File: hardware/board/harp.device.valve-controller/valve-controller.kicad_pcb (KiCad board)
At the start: 4 copper layers, 80 x 168 mm, 149 parts, among them J1 Screw_Terminal_01x02, J10 Screw_Terminal_01x02, J11 Screw_Terminal_01x02, J12 Screw_Terminal_01x02, J13 Screw_Terminal_01x02, J14 Screw_Terminal_01x02, J15 Screw_Terminal_01x02, J16 Screw_Terminal_01x02, J17 Screw_Terminal_01x02, J18 Screw_Terminal_01x02, J19 Screw_Terminal_01x02, J2 Conn_01x03_Male, J20 Screw_Terminal_01x02, J3 Screw_Terminal_01x02, J4 AudioJack3, J5 USB_C_Receptacle_USB2.0, J6 Screw_Terminal_01x02, J7 Screw_Terminal_01x02, J8 Screw_Terminal_01x02, J9 Screw_Terminal_01x02, Q2 GSFD4005, U1 MIC4127, U10 MIC4127, U11 MIC4127, U12 MIC4127, U13 MIC4127, U14 MIC4127, U2 TPD2EUSB30, U3 ADUM4160, U4 RP2040, U5 W25Q16JVUXIQ, U6 MIC4127, U7 rt6150b-33gqw, U8 MIC4127, U9 MCP16312x-xMNY, X1 ECS-TXO-2016

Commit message: route pcb
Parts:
- removed G3: LOGO, LOGO
- added G***: LOGO, LOGO, B.Cu at (131.9, 166.4)
- added J26: Conn_02x10_Odd_Even, Connector_PinHeader_2.54mm:PinHeader_2x10_P2.54mm_Vertical_SMD, F.Cu at (122.8, 115.0)
- added REF**: MountingHole_3.2mm_M3_DIN965, MountingHole:MountingHole_3.2mm_M3_DIN965, F.Cu at (105.8, 181.0)
- added REF**: MountingHole_3.2mm_M3_DIN965, MountingHole:MountingHole_3.2mm_M3_DIN965, F.Cu at (105.8, 112.0)
- added REF**: MountingHole_3.2mm_M3_DIN965, MountingHole:MountingHole_3.2mm_M3_DIN965, F.Cu at (139.8, 112.0)
- J4: moved to F.Cu
- moved REF1 151.7 mm to (133.8, 180.5)
- moved C11 66.8 mm to (100.7, 102.6), turned to -90 degrees
- moved C16 61.9 mm to (108.7, 106.3), turned to 135 degrees
- moved U7 49.5 mm to (135.1, 74.6), turned to 180 degrees
- moved R15 47.6 mm to (131.4, 74.0), turned to -90 degrees
- moved C28 46.8 mm to (135.1, 77.3)
- moved R16 45.9 mm to (132.4, 74.6), turned to -90 degrees
- moved L3 45.3 mm to (137.8, 74.5), turned to -90 degrees
- moved C27 45.0 mm to (139.9, 73.6), turned to -90 degrees
- moved R20 27.6 mm to (124.8, 32.8), turned to 90 degrees
- moved C32 27.1 mm to (121.8, 34.6), turned to 90 degrees
- moved C33 25.3 mm to (128.0, 36.5), turned to -90 degrees
- moved R19 25.1 mm to (127.2, 33.5), turned to 180 degrees
- moved C30 24.0 mm to (124.6, 40.8)
- moved C31 23.4 mm to (124.6, 38.8)
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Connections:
- C20 pad 2: VPP -> +5V
- C21 pad 2: VPP -> +5V
- C22 pad 2: VPP -> +5V
- C23 pad 2: VPP -> +5V
- C24 pad 2: VPP -> +5V
- C25 pad 2: VPP -> +5V
- C26 pad 2: VPP -> +5V
- C28 pad 2: +3V3 -> +3.3V
- C29 pad 2: VPP -> +5V
- R12 pad 1: Net-(U4-GPIO24) -> Net-(U4-GPIO2)
- R13 pad 1: Net-(U4-GPIO25) -> Net-(U4-GPIO3)
- U1 pad 6: VPP -> +5V
- U10 pad 6: VPP -> +5V
- U11 pad 6: VPP -> +5V
- U12 pad 6: VPP -> +5V
- U13 pad 6: VPP -> +5V
- U14 pad 6: VPP -> +5V
- U4 pad 34: unconnected-(U4-GPIO22-Pad34) -> /Harp Core RP2040 + Isolated USB/GPIO0
- U4 pad 35: unconnected-(U4-GPIO23-Pad35) -> /Harp Core RP2040 + Isolated USB/GPIO1
- U4 pad 36: Net-(U4-GPIO24) -> /Harp Core RP2040 + Isolated USB/GPIO2
- U4 pad 37: Net-(U4-GPIO25) -> /Harp Core RP2040 + Isolated USB/GPIO3
- U4 pad 38: unconnected-(U4-GPIO26_ADC0-Pad38) -> /Harp Core RP2040 + Isolated USB/GPIO4
- U4 pad 39: unconnected-(U4-GPIO27_ADC1-Pad39) -> /Harp Core RP2040 + Isolated USB/GPIO5
- U4 pad 4: unconnected-(U4-GPIO2-Pad4) -> Net-(U4-GPIO2)
- U4 pad 40: unconnected-(U4-GPIO28_ADC2-Pad40) -> /Harp Core RP2040 + Isolated USB/GPIO6
- U4 pad 41: unconnected-(U4-GPIO29_ADC3-Pad41) -> /Harp Core RP2040 + Isolated USB/GPIO7
- U4 pad 5: unconnected-(U4-GPIO3-Pad5) -> Net-(U4-GPIO3)
- U6 pad 6: VPP -> +5V
- U7 pad 1: +3V3 -> +3.3V
- U7 pad 10: +3V3 -> +3.3V
- U8 pad 6: VPP -> +5V
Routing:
- net VPP: track 0.00 -> 77.8 mm, vias 0 -> 9
- net GND: track 25.6 -> 101.8 mm, vias 29 -> 92
- net /Harp Core RP2040 + Isolated USB/OUT15: track 0.00 -> 74.7 mm, vias 0 -> 2
- net /Harp Core RP2040 + Isolated USB/OUT14: track 0.00 -> 71.8 mm, vias 0 -> 2
- net /Harp Core RP2040 + Isolated USB/OUT0: track 0.00 -> 71.1 mm
- net /Harp Core RP2040 + Isolated USB/OUT1: track 0.00 -> 69.2 mm
- net /Harp Core RP2040 + Isolated USB/OUT13: track 0.00 -> 53.0 mm
- net /Harp Core RP2040 + Isolated USB/OUT12: track 0.00 -> 51.0 mm
- net /Harp Core RP2040 + Isolated USB/OUT2: track 0.00 -> 50.8 mm
- net /Harp Core RP2040 + Isolated USB/OUT3: track 0.00 -> 48.8 mm
- net Net-(U4-GPIO25): track 42.5 -> 0.00 mm, vias 2 -> 0
- net Net-(U4-GPIO2): track 0.00 -> 36.0 mm, vias 0 -> 2
- net +5V: track 0.00 -> 32.4 mm, vias 0 -> 27
- net Net-(U4-GPIO24): track 31.9 -> 0.00 mm, vias 2 -> 0
- net Net-(U4-GPIO3): track 0.00 -> 31.2 mm, vias 0 -> 2
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- added copper zone on F.Cu, net +1V1
- added copper zone on In2.Cu, net +3.3V
- added copper zone on F.Cu, net +5V
- added copper zone on In2.Cu, net +5V
- added copper zone on F.Cu, net GND1
- added copper zone on F.Cu, net Net-(D10-A)
- added copper zone on F.Cu, net Net-(D11-A)
- added copper zone on F.Cu, net Net-(D12-A)
- added copper zone on F.Cu, net Net-(D13-A)
- added copper zone on F.Cu, net Net-(D14-A)
- added copper zone on F.Cu, net Net-(D15-A)
- added copper zone on F.Cu, net Net-(D16-A)
- added copper zone on F.Cu, net Net-(D17-A)
- added copper zone on F.Cu, net Net-(D18-A)
- added copper zone on F.Cu, net Net-(D19-A)
- added copper zone on F.Cu, net Net-(D20-A)
- added copper zone on F.Cu, net Net-(D21-A)
- added copper zone on F.Cu, net Net-(D5-A)
- added copper zone on F.Cu, net Net-(D6-A)
- added copper zone on F.Cu, net Net-(D7-A)
- added copper zone on F.Cu, net Net-(D8-A)
- added copper zone on F.Cu, net Net-(D9-A)
- added copper zone on F.Cu, net Net-(D9-K)
- added copper zone on F.Cu, net Net-(U9-SW)
- added copper zone on F.Cu, net VPP
- added copper zone on In2.Cu, net VPP
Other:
- board size 80 x 168 mm -> 70 x 168 mm
- board text added: "0368-E-001-001.000.000"
- board text added: "6-24VDC 5A Max"
- board text added: "Harp Sync Input"
- board text added: "Sonya Vasquez Feb 6, 2025"
- board text added: "Source Files & Setup"
- board text added: "harp.device.valve-controller"
- board text removed: "* 16 valve outputs * 4 camera triggers * 4 Poke inputs"
- board text removed: "2.1 x 5.5mm"
- board text removed: "6-20VDC"
- board text removed: "Sonya Vasquez"
- board text removed: "Source Files & Setup →"
- board text removed: "↑ Harp Sync Input"

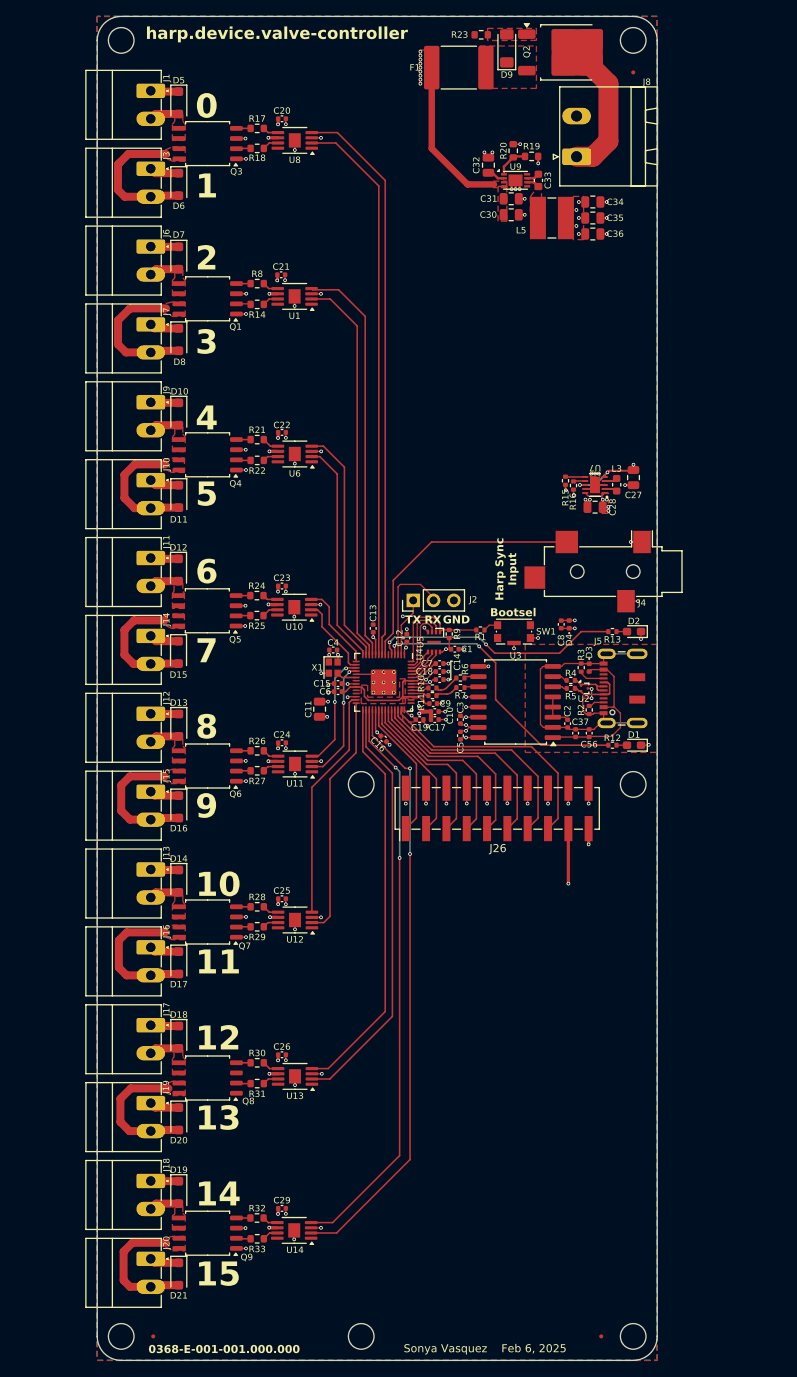
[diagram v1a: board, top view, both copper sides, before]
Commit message: update pcb power supply
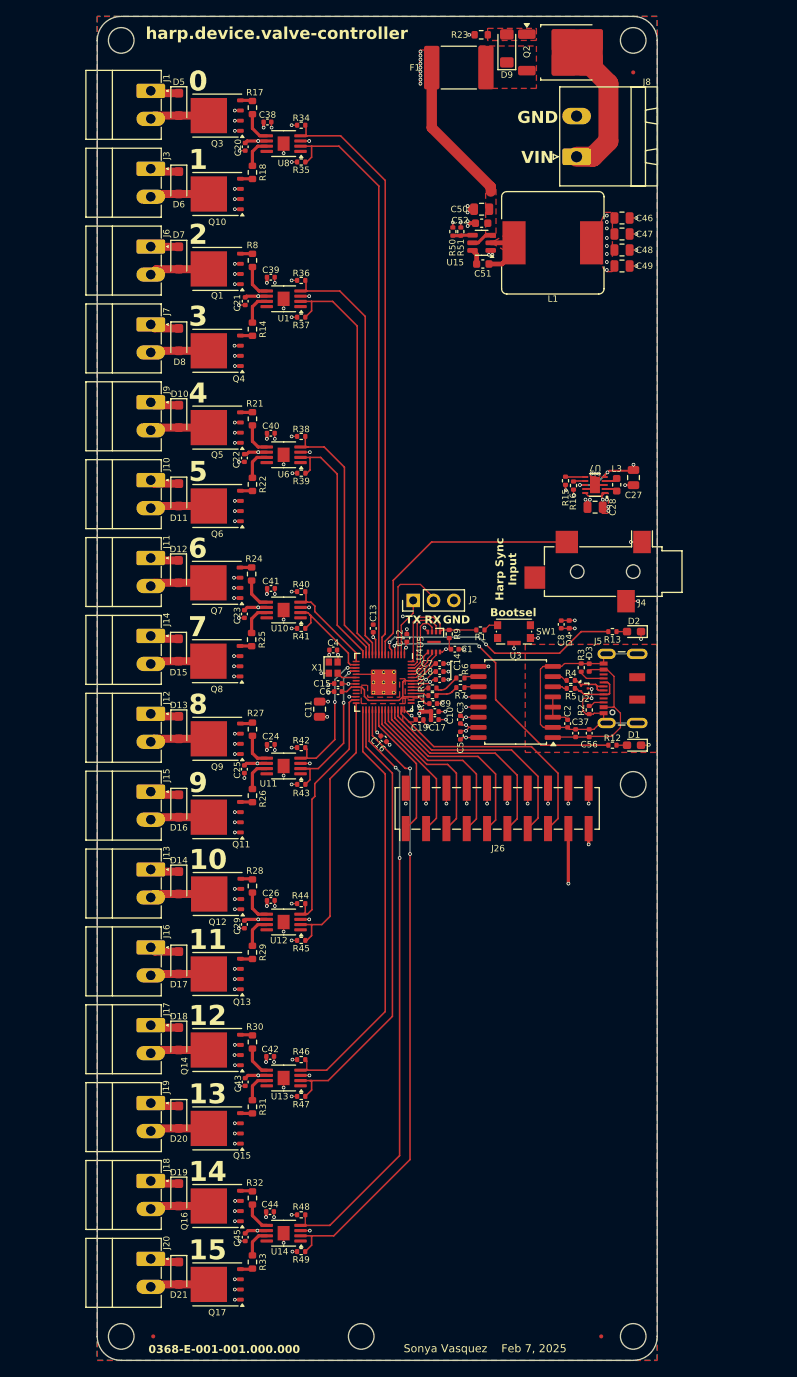
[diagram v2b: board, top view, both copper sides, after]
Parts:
- removed C30: 3.3uF, Capacitor_SMD:C_0805_2012Metric
- removed C31, C34, C35, C36: 10uF, Capacitor_SMD:C_0805_2012Metric
- removed C32: 1uF, Capacitor_SMD:C_0805_2012Metric
- removed C33: 0.1uF, Capacitor_SMD:C_0603_1608Metric
- removed L5: 15uH, kicad_component_library:L_Wuerth_5.5x5.3mm
- removed R19: 52K3, Resistor_SMD:R_0603_1608Metric
- removed R20: 10K, Resistor_SMD:R_0603_1608Metric
- removed U9: MCP16312x-xMNY, Package_DFN_QFN:DFN-8-1EP_3x2mm_P0.5mm_EP1.75x1.45mm
- added C38: 1uF, Capacitor_SMD:C_0402_1005Metric, F.Cu at (94.1, 29.2)
- added C39: 1uF, Capacitor_SMD:C_0402_1005Metric, F.Cu at (94.5, 48.6)
- added C40: 1uF, Capacitor_SMD:C_0402_1005Metric, F.Cu at (94.5, 68.1)
- added C41: 1uF, Capacitor_SMD:C_0402_1005Metric, F.Cu at (94.6, 87.5)
- added C42: 1uF, Capacitor_SMD:C_0402_1005Metric, F.Cu at (94.5, 146.0)
- added C43: 100nF, Capacitor_SMD:C_0402_1005Metric, F.Cu at (91.3, 149.2)
- added C44: 1uF, Capacitor_SMD:C_0402_1005Metric, F.Cu at (94.5, 165.4)
- added C45: 100nF, Capacitor_SMD:C_0402_1005Metric, F.Cu at (91.3, 168.6)
- added C46: 10uF, Capacitor_SMD:C_0805_2012Metric, F.Cu at (138.4, 41.2)
- added C47: 10uF, Capacitor_SMD:C_0805_2012Metric, F.Cu at (138.4, 43.2)
- added C48: 10uF, Capacitor_SMD:C_0805_2012Metric, F.Cu at (138.4, 45.2)
- added C49: 10uF, Capacitor_SMD:C_0805_2012Metric, F.Cu at (138.4, 47.2)
- added C50: 10uF, Capacitor_SMD:C_0805_2012Metric, F.Cu at (120.9, 40.1)
- added C51: 0.1uF, Capacitor_SMD:C_0603_1608Metric, F.Cu at (121.0, 47.0)
- added C52: 0.1uF, Capacitor_SMD:C_0603_1608Metric, F.Cu at (120.9, 41.9)
- added L1: 6.8uH, Inductor_SMD:L_Bourns_SRR1260, F.Cu at (129.8, 44.3)
- added Q10: CSD17570Q5B, Package_TO_SOT_SMD:TDSON-8-1, F.Cu at (87.8, 38.2)
- added Q11: CSD17570Q5B, Package_TO_SOT_SMD:TDSON-8-1, F.Cu at (87.8, 116.1)
- added Q12: CSD17570Q5B, Package_TO_SOT_SMD:TDSON-8-1, F.Cu at (87.9, 125.7)
- added Q13: CSD17570Q5B, Package_TO_SOT_SMD:TDSON-8-1, F.Cu at (87.8, 135.7)
- added Q14: CSD17570Q5B, Package_TO_SOT_SMD:TDSON-8-1, F.Cu at (87.8, 145.2)
- added Q15: CSD17570Q5B, Package_TO_SOT_SMD:TDSON-8-1, F.Cu at (87.8, 155.0)
- added Q16: CSD17570Q5B, Package_TO_SOT_SMD:TDSON-8-1, F.Cu at (87.8, 164.7)
- added Q17: CSD17570Q5B, Package_TO_SOT_SMD:TDSON-8-1, F.Cu at (87.8, 174.5)
- added R34: 10K, Resistor_SMD:R_0402_1005Metric, F.Cu at (98.3, 29.6)
- added R35: 10K, Resistor_SMD:R_0402_1005Metric, F.Cu at (98.3, 34.2)
- added R36: 10K, Resistor_SMD:R_0402_1005Metric, F.Cu at (98.3, 49.0)
- added R37: 10K, Resistor_SMD:R_0402_1005Metric, F.Cu at (98.3, 53.6)
- added R38: 10K, Resistor_SMD:R_0402_1005Metric, F.Cu at (98.3, 68.5)
- added R39: 10K, Resistor_SMD:R_0402_1005Metric, F.Cu at (98.4, 73.1)
- added R40: 10K, Resistor_SMD:R_0402_1005Metric, F.Cu at (98.3, 87.9)
- added R41: 10K, Resistor_SMD:R_0402_1005Metric, F.Cu at (98.3, 92.5)
- added R42: 10K, Resistor_SMD:R_0402_1005Metric, F.Cu at (98.3, 107.4)
- added R43: 10K, Resistor_SMD:R_0402_1005Metric, F.Cu at (98.4, 112.0)
- added R44: 10K, Resistor_SMD:R_0402_1005Metric, F.Cu at (98.3, 126.9)
- added R45: 10K, Resistor_SMD:R_0402_1005Metric, F.Cu at (98.3, 131.5)
- added R46: 10K, Resistor_SMD:R_0402_1005Metric, F.Cu at (98.3, 146.4)
- added R47: 10K, Resistor_SMD:R_0402_1005Metric, F.Cu at (98.3, 151.0)
- added R48: 10K, Resistor_SMD:R_0402_1005Metric, F.Cu at (98.3, 165.8)
- added R49: 10K, Resistor_SMD:R_0402_1005Metric, F.Cu at (98.3, 170.4)
- added R50: 100K, Resistor_SMD:R_0402_1005Metric, F.Cu at (117.3, 42.9)
- added R51: 13K7, Resistor_SMD:R_0402_1005Metric, F.Cu at (118.3, 42.9)
- added U15: LMR51430, Package_TO_SOT_SMD:SOT-23-6, F.Cu at (120.9, 44.3)
- C24, C26: value 100nF -> 1uF
- Q1, Q3, Q4, Q5, Q6, Q7, Q8, Q9: value ~ -> CSD17570Q5B; footprint Package_SO:SOIC-8_5.275x5.275mm_P1.27mm -> Package_TO_SOT_SMD:TDSON-8-1
- moved Q9 61.8 mm to (87.8, 106.3)
- moved Q8 52.1 mm to (87.8, 96.6)
- moved Q7 42.4 mm to (87.8, 86.8)
- moved C29 35.8 mm to (91.2, 129.5), turned to 90 degrees
- moved Q6 32.5 mm to (87.8, 77.2)
- moved Q5 22.9 mm to (87.8, 67.4)
- moved C26 19.4 mm to (94.5, 126.5), turned to 0 degrees
- moved C25 16.9 mm to (91.2, 110.1), turned to 90 degrees
- moved Q4 13.1 mm to (87.8, 57.8)
- moved C23 5.86 mm to (91.2, 90.7), turned to 90 degrees
- moved C20 5.78 mm to (91.3, 32.3), turned to 90 degrees
- moved C22 5.69 mm to (91.2, 71.2), turned to 90 degrees
- moved R26 5.63 mm to (92.2, 113.4), turned to -90 degrees
- moved C21 5.58 mm to (91.3, 51.6), turned to 90 degrees
- moved R27 5.23 mm to (92.2, 105.1), turned to 90 degrees
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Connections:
- C24 pad 1: GND -> +5V
- C24 pad 2: +5V -> GND
- C26 pad 1: GND -> +5V
- C26 pad 2: +5V -> GND
- Q1 pad 2: /Valve Control/CTRL4 -> GND
- Q3 pad 2: /Valve Control/CTRL2 -> GND
- Q4 pad 2: /Valve Control/CTRL6 -> GND
- Q4 pad 4: /Valve Control/CTRL5 -> /Valve Control/CTRL4
- Q4 pad 5: Net-(D10-A) -> Net-(D8-A)
- Q5 pad 2: /Valve Control/CTRL8 -> GND
- Q5 pad 4: /Valve Control/CTRL7 -> /Valve Control/CTRL5
- Q5 pad 5: Net-(D12-A) -> Net-(D10-A)
- Q6 pad 2: /Valve Control/CTRL10 -> GND
- Q6 pad 4: /Valve Control/CTRL9 -> /Valve Control/CTRL6
- Q6 pad 5: Net-(D13-A) -> Net-(D11-A)
- Q7 pad 2: /Valve Control/CTRL12 -> GND
- Q7 pad 4: /Valve Control/CTRL11 -> /Valve Control/CTRL7
- Q7 pad 5: Net-(D14-A) -> Net-(D12-A)
- Q8 pad 2: /Valve Control/CTRL14 -> GND
- Q8 pad 4: /Valve Control/CTRL13 -> /Valve Control/CTRL8
- Q8 pad 5: Net-(D18-A) -> Net-(D15-A)
- Q9 pad 2: /Valve Control/CTRL16 -> GND
- Q9 pad 4: /Valve Control/CTRL15 -> /Valve Control 2/CTRL9
- Q9 pad 5: Net-(D19-A) -> Net-(D13-A)
- R26 pad 1: Net-(U11-OUT_B) -> Net-(U11-OUT_A)
- R26 pad 2: /Valve Control/CTRL9 -> /Valve Control 2/CTRL10
- R27 pad 1: Net-(U11-OUT_A) -> Net-(U11-OUT_B)
- R27 pad 2: /Valve Control/CTRL10 -> /Valve Control 2/CTRL9
- R28 pad 2: /Valve Control/CTRL11 -> /Valve Control 2/CTRL11
- R29 pad 2: /Valve Control/CTRL12 -> /Valve Control 2/CTRL12
- R30 pad 2: /Valve Control/CTRL13 -> /Valve Control 2/CTRL13
- R31 pad 2: /Valve Control/CTRL14 -> /Valve Control 2/CTRL14
- R32 pad 2: /Valve Control/CTRL15 -> /Valve Control 2/CTRL15
- R33 pad 2: /Valve Control/CTRL16 -> /Valve Control 2/CTRL16
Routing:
- net GND: track 101.8 -> 135.6 mm, vias 92 -> 151
- net +5V: track 32.4 -> 46.2 mm, vias 27 -> 30
- net Net-(D8-A): track 17.7 -> 7.34 mm
- net Net-(D6-A): track 17.7 -> 7.40 mm
- net Net-(D17-A): track 17.6 -> 7.33 mm
- net Net-(D20-A): track 17.3 -> 7.39 mm
- net Net-(D16-A): track 16.8 -> 7.38 mm
- net Net-(D21-A): track 16.7 -> 7.38 mm
- net Net-(D11-A): track 15.9 -> 7.37 mm
- net Net-(D15-A): track 15.8 -> 7.35 mm
- net Net-(U15-SW): track 0.00 -> 7.81 mm
- net /Harp Core RP2040 + Isolated USB/OUT9: track 15.5 -> 20.2 mm
- net Net-(U9-Vfb): track 4.12 -> 0.00 mm
- net /Harp Core RP2040 + Isolated USB/OUT13: track 53.0 -> 57.0 mm
- net /Harp Core RP2040 + Isolated USB/OUT11: track 30.6 -> 34.5 mm
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- added copper zone on F.Cu, net Net-(U15-SW)
- removed copper zone on F.Cu, net Net-(D10-A)
- removed copper zone on F.Cu, net Net-(D11-A)
- removed copper zone on F.Cu, net Net-(D12-A)
- removed copper zone on F.Cu, net Net-(D13-A)
- removed copper zone on F.Cu, net Net-(D14-A)
- removed copper zone on F.Cu, net Net-(D15-A)
- removed copper zone on F.Cu, net Net-(D16-A)
- removed copper zone on F.Cu, net Net-(D17-A)
- removed copper zone on F.Cu, net Net-(D18-A)
- removed copper zone on F.Cu, net Net-(D19-A)
- removed copper zone on F.Cu, net Net-(D20-A)
- removed copper zone on F.Cu, net Net-(D21-A)
- removed copper zone on F.Cu, net Net-(D5-A)
- removed copper zone on F.Cu, net Net-(D6-A)
- removed copper zone on F.Cu, net Net-(D7-A)
- removed copper zone on F.Cu, net Net-(D8-A)
- removed copper zone on F.Cu, net Net-(U9-SW)
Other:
- board text added: "5-24VDC 5A"
- board text added: "Limits: * 5A max combined channel current. * 2A max any one channel."
- board text added: "Sonya Vasquez Feb 7, 2025"
- board text added: "V+"
- board text added: "V-"
- board text added: "VIN"
- board text removed: "6-24VDC 5A Max"
- board text removed: "Sonya Vasquez Feb 6, 2025"

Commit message: update bom
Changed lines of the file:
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@@
 		(tags "RT6150B-33GQW ")
 		(property "Reference" "U7"
-			(at -0.0154 2.1272 180)
+			(at -0.0154 2.072802 0)
 			(unlocked yes)
 			(layer "F.SilkS")
@@
 		(polygon
 			(pts
-				(xy 135.9346 75.545602) (xy 135.9346 78.120602) (xy 136.75 78.120602) (xy 136.7346 75.545602)
+				(xy 135.9346 75.445602) (xy 135.9346 78.020602) (xy 136.75 78.020602) (xy 136.7346 75.445602)
 			)
 		)

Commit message: prep hw initial release
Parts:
- removed C49: 10uF, Capacitor_SMD:C_0805_2012Metric
- added J21: Conn_01x03_Male, Connector_PinHeader_2.54mm:PinHeader_1x03_P2.54mm_Vertical, F.Cu at (97.5, 97.5)
- C46, C47, C48: value 10uF -> 22uF
- C51, C52: value 0.1uF -> 100nF; footprint Capacitor_SMD:C_0603_1608Metric -> Capacitor_SMD:C_0402_1005Metric
- R23: footprint Resistor_SMD:R_0603_1608Metric -> Resistor_SMD:R_0402_1005Metric
- moved C11 1.68 mm to (101.0, 104.2)
- moved C46 1.10 mm to (138.5, 42.3), turned to 180 degrees
- moved C47 1.10 mm to (138.5, 44.3), turned to 180 degrees
- moved C48 1.10 mm to (138.5, 46.3), turned to 180 degrees
- moved C15 0.63 mm to (102.3, 99.2)
- moved C6 0.63 mm to (102.3, 100.2)
- moved C1 0.40 mm to (117.3, 95.5)
- moved R50 0.30 mm to (117.3, 43.2)
- moved R51 0.30 mm to (118.3, 43.2)
- moved C4 0.28 mm to (102.2, 95.4)
- moved C51 0.25 mm to (121.0, 46.7), turned to 180 degrees
- moved X1 0.22 mm to (102.2, 97.3)
- moved R23 0.20 mm to (121.0, 18.3)
- turned R9 to 90 degrees
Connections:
- C46 pad 1: +5V -> GND
- C46 pad 2: GND -> +5V
- C47 pad 1: +5V -> GND
- C47 pad 2: GND -> +5V
- C48 pad 1: +5V -> GND
- C48 pad 2: GND -> +5V
- C51 pad 1: Net-(U15-CB) -> Net-(U15-SW)
- C51 pad 2: Net-(U15-SW) -> Net-(U15-CB)
- R9 pad 1: /Harp Core RP2040 + Isolated USB/QSPI_CS -> +3.3V
- R9 pad 2: +3.3V -> /Harp Core RP2040 + Isolated USB/QSPI_CS
- U4 pad 24: unconnected-(U4-SWCLK-Pad24) -> Net-(J21-Pin_1)
- U4 pad 25: unconnected-(U4-SWD-Pad25) -> Net-(J21-Pin_2)
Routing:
- net Net-(J21-Pin_1): track 0.00 -> 9.50 mm
- net Net-(J21-Pin_2): track 0.00 -> 8.66 mm
- net GND: track 135.6 -> 133.9 mm, vias 151 -> 150
- net +3.3V: track 44.4 -> 43.7 mm
- net +5V: track 46.2 -> 46.1 mm, vias 30 -> 28
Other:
- board text added: "SWCLK"
- board text added: "SWD"
- board text added: "Sonya Vasquez Feb 11, 2025"
- board text removed: "Sonya Vasquez Feb 7, 2025"

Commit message: update silkscreen w/ gpio descriptions
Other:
- board text added: "----- GND -----"
- board text added: "3.3V"
- board text added: "5V"
- board text added: "GPIO22"
- board text added: "GPIO23"
- board text added: "GPIO24"
- board text added: "GPIO25"
- board text added: "GPIO26"
- board text added: "GPIO27"
- board text added: "GPIO28"
- board text added: "GPIO29"
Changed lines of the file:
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@@
 		(tags "Surface mounted pin header SMD 2x10 2.54mm double row")
 		(property "Reference" "J26"
-			(at -5 0.1 180)
+			(at -0.2 -11.4 180)
 			(layer "F.SilkS")
 			(effects
@@
 		)
 	)
+	(gr_text "GPIO26"
+		(at 122.55 129.2 90)
+		(layer "F.SilkS")
+		(effects
+			(font
+				(size 1.5 1.5)
+				(thickness 0.3)
+				(bold yes)
+			)
+			(justify left bottom)
+		)
+	)
+	(gr_text "----- GND -----"
+		(at 109.95 109.9 0)
+		(layer "F.SilkS")
+		(effects
+			(font
+				(size 1.5 1.5)
+				(thickness 0.3)
+				(bold yes)
+			)
+			(justify left bottom)
+		)
+	)
+	(gr_text "GPIO23"
+		(at 114.85 129.2 90)
+		(layer "F.SilkS")
+		(effects
+			(font
+				(size 1.5 1.5)
+				(thickness 0.3)
+				(bold yes)
+			)
+			(justify left bottom)
+		)
+	)
 	(gr_text "14"
 		(at 84.27 161.87 0)
@@
 		)
 	)
+	(gr_text "3.3V"
+		(at 135.15 126.2 90)
+		(layer "F.SilkS")
+		(effects
+			(font
+				(size 1.5 1.5)
+				(thickness 0.3)
+				(bold yes)
+			)
+			(justify left bottom)
+		)
+	)
+	(gr_text "GPIO27"
+		(at 125.05 129.2 90)
+		(layer "F.SilkS")
+		(effects
+			(font
+				(size 1.5 1.5)
+				(thickness 0.3)
+				(bold yes)
+			)
+			(justify left bottom)
+		)
+	)
 	(gr_text "15"
 		(at 84.27 171.67 0)
@@
 		)
 	)
+	(gr_text "GPIO28"
+		(at 127.65 129.2 90)
+		(layer "F.SilkS")
+		(effects
+			(font
+				(size 1.5 1.5)
+				(thickness 0.3)
+				(bold yes)
+			)
+			(justify left bottom)
+		)
+	)
 	(gr_text "SWCLK"
 		(at 91.75 98 0)
@@
 		)
 	)
+	(gr_text "GPIO29"
+		(at 130.15 129.2 90)
+		(layer "F.SilkS")
+		(effects
+			(font
+				(size 1.5 1.5)
+				(thickness 0.3)
+				(bold yes)
+			)
+			(justify left bottom)
+		)
+	)
 	(gr_text "1"
 		(at 84.27 35.37 0)
@@
 		)
 	)
+	(gr_text "GPIO25"
+		(at 119.95 129.2 90)
+		(layer "F.SilkS")
+		(effects
+			(font
+				(size 1.5 1.5)
+				(thickness 0.3)
+				(bold yes)
+			)
+			(justify left bottom)
+		)
+	)
 	(gr_text "harp.device.valve-controller"
 		(at 78.9 19 0)
@@
 		)
 	)
+	(gr_text "GPIO22"
+		(at 112.25 129.2 90)
+		(layer "F.SilkS")
+		(effects
+			(font
+				(size 1.5 1.5)
+				(thickness 0.3)
+				(bold yes)
+			)
+			(justify left bottom)
+		)
+	)
 	(gr_text "4"
 		(at 84.27 64.57 0)
@@
 		)
 	)
+	(gr_text "5V"
+		(at 132.75 124 90)
+		(layer "F.SilkS")
+		(effects
+			(font
+				(size 1.5 1.5)
+				(thickness 0.3)
+				(bold yes)
+			)
+			(justify left bottom)
+		)
+	)
 	(gr_text "GND"
 		(at 93.15 103.1 0)
@@
 				(bold yes)
 			)
+			(justify left bottom)
+		)
+	)
+	(gr_text "GPIO24"
+		(at 117.45 129.2 90)
+		(layer "F.SilkS")
+		(effects
+			(font
+				(size 1.5 1.5)
+				(thickness 0.3)
+				(bold yes)
+			)
